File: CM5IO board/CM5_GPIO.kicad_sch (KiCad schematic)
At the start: 21 parts, among them J14 JST_SHBM04B-SRSS-TB, J2 Conn_02x07_Odd_Even, J3 Conn_01x03, J7 Micro_SD_Card_Det, J8 THD-20-R, SW1 Right angle Tact button, U18 RT9742GGJ5

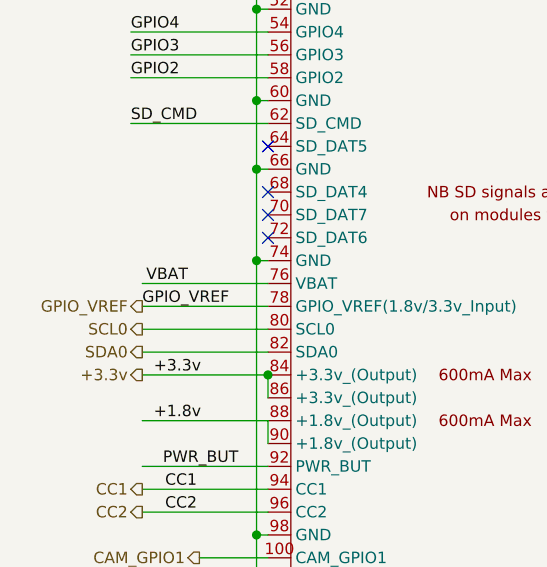
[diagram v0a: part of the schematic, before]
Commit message: Blocked off vbat
still need to block off ethernet
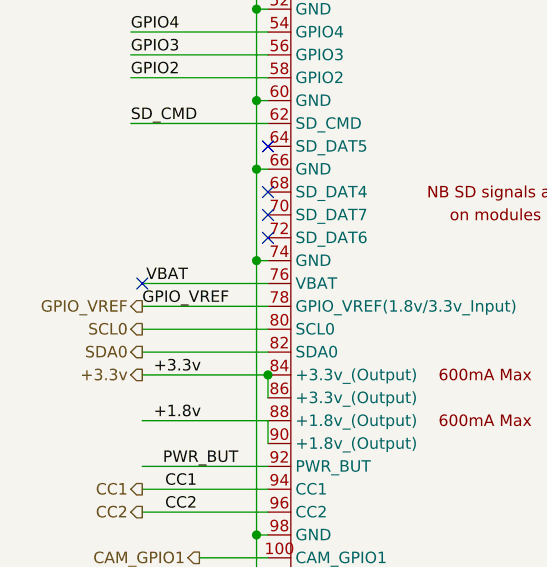
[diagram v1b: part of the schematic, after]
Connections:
- no-connect marks 9 -> 10
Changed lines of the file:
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@@
+	)
+	(no_connect
+		(at 25.4 115.57)
 	)
 	(no_connect
